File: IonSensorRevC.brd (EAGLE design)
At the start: 50.8 x 22.9 mm, 19 parts, among them U1 REF2033AIDDCT, U2 INA826AIDR, U3 INA826AIDR, U4 INA826AIDR, X1 SFV4R-1STE1LF

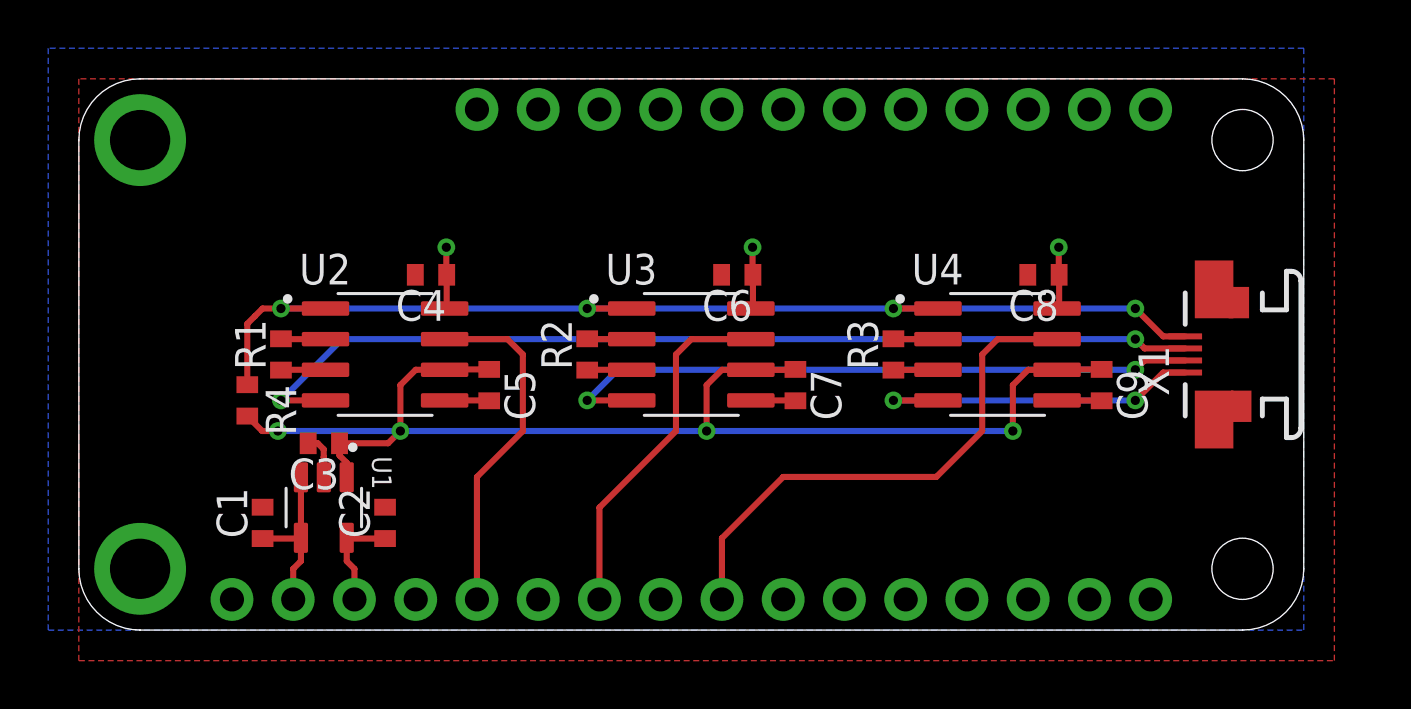
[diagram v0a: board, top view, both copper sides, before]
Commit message: Update traces
Updated traces to minimize noise
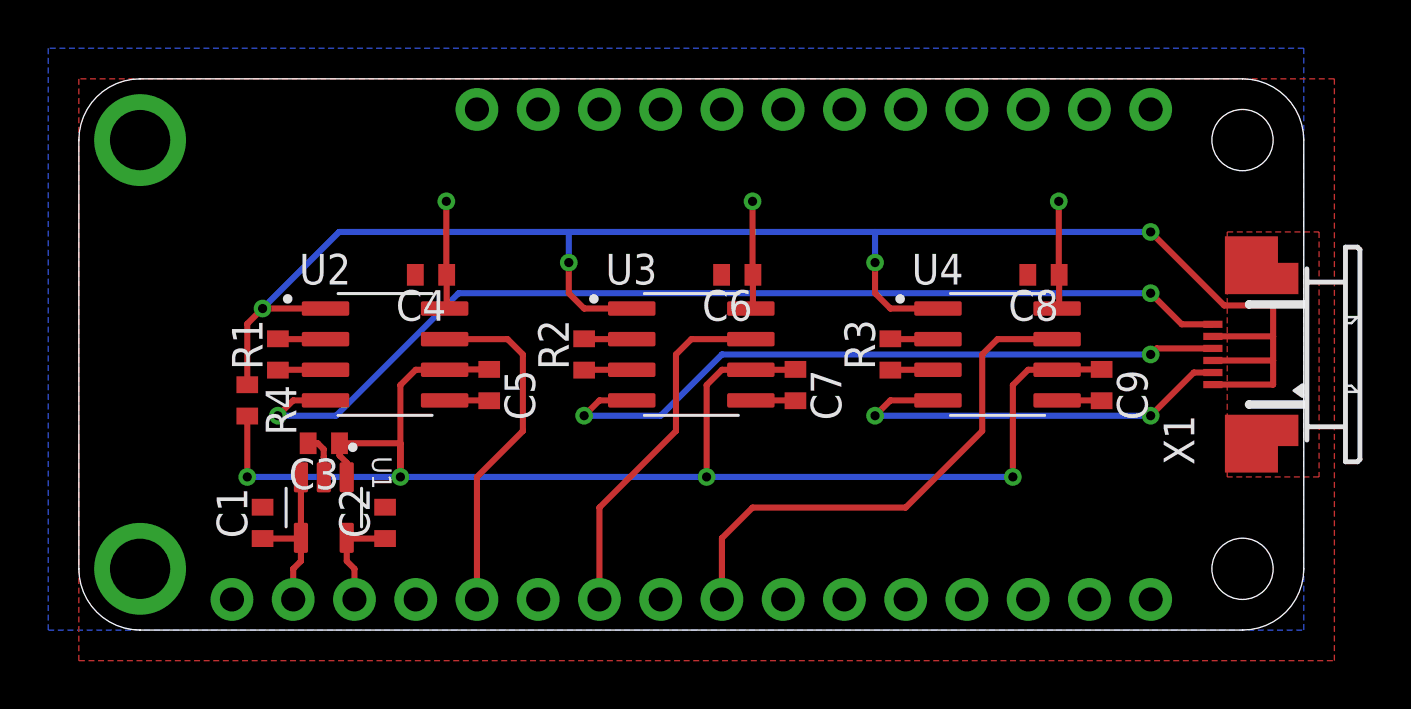
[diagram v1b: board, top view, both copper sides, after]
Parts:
- X1: value SFV4R-1STE1LF -> 52745-0690; device adafruit:SFV4R-1STE1LF -> con-molex:52745-0690
- moved X1 3.05 mm to (49.5, 11.4)
- moved R2 0.13 mm to (21.0, 11.4)
- moved R1 0.13 mm to (8.26, 11.4)
- moved R3 0.13 mm to (33.7, 11.4)
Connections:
- removed net A1: MS1.6
- removed net A3: MS1.8
- removed net A5: MS1.10
- removed net CH1: U3.4, X1.2
- new net CH4: U4.4, X1.2
- net CH0: now also X1.6; no longer X1.3
- net CH2: now also U3.4, X1.4; no longer U4.4, X1.1
- net GND: now also MS1.10, MS1.6, MS1.8
- net REF: now also X1.1, X1.3, X1.5; no longer X1.4
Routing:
- net CH1: track 27.3 -> 0.00 mm, vias 2 -> 0
- net REF: track 47.7 -> 72.1 mm
- net CH4: track 0.00 -> 17.6 mm, vias 0 -> 2
- net CH2: track 14.4 -> 29.5 mm
- net VCC/2: track 53.9 -> 63.0 mm
- net +3V3: track 14.5 -> 20.3 mm
- net CH0: track 40.6 -> 43.7 mm
- added copper zone on layer 1, net REF
